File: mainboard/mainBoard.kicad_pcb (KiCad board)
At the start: 4 copper layers, 110 x 75 mm, 85 parts, among them IC1 TCAN3414DR, J1 XT60PW-M, J10 XT30U-M, J11 XT30U-M, J12 Conn_01x03, J13 BM02B-SRSS-TB, J14 BM02B-SRSS-TB, J15 BM02B-SRSS-TB, J16 BM04B-SRSS-TB, J17 BM04B-SRSS-TB, J18 BM04B-SRSS-TB, J19 BM04B-SRSS-TB, J2 XT60PW-M, J20 BM04B-SRSS-TB, J21 B2B-PH_K, J22 Conn_01x02, J23 Conn_02x04_Odd_Even, J24 BM02B-SRSS-TB, J25 BM02B-SRSS-TB, J26 BM02B-SRSS-TB, J3 XT30PW-M, J4 XT30PW-M, J5 Barrel_Jack, J6 XT30U_M, J7 XT30U-M, J8 XT30U-M, J9 XT30U-M, Q1 FQD11P06TM, Q2 FQD11P06TM, U1 TPS565208, U2 TPS565208, U3 TCA9548APWR

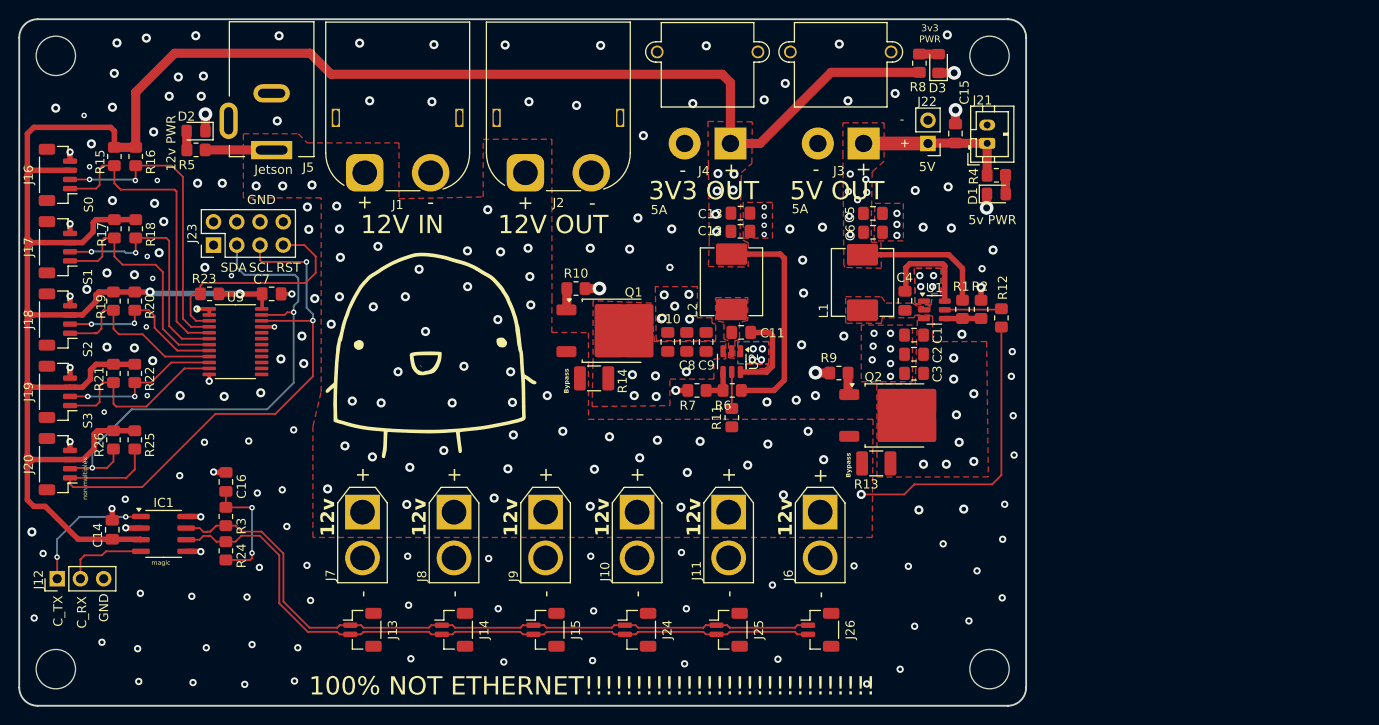
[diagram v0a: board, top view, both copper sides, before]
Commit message: layed out PCB, started routing of mainboard
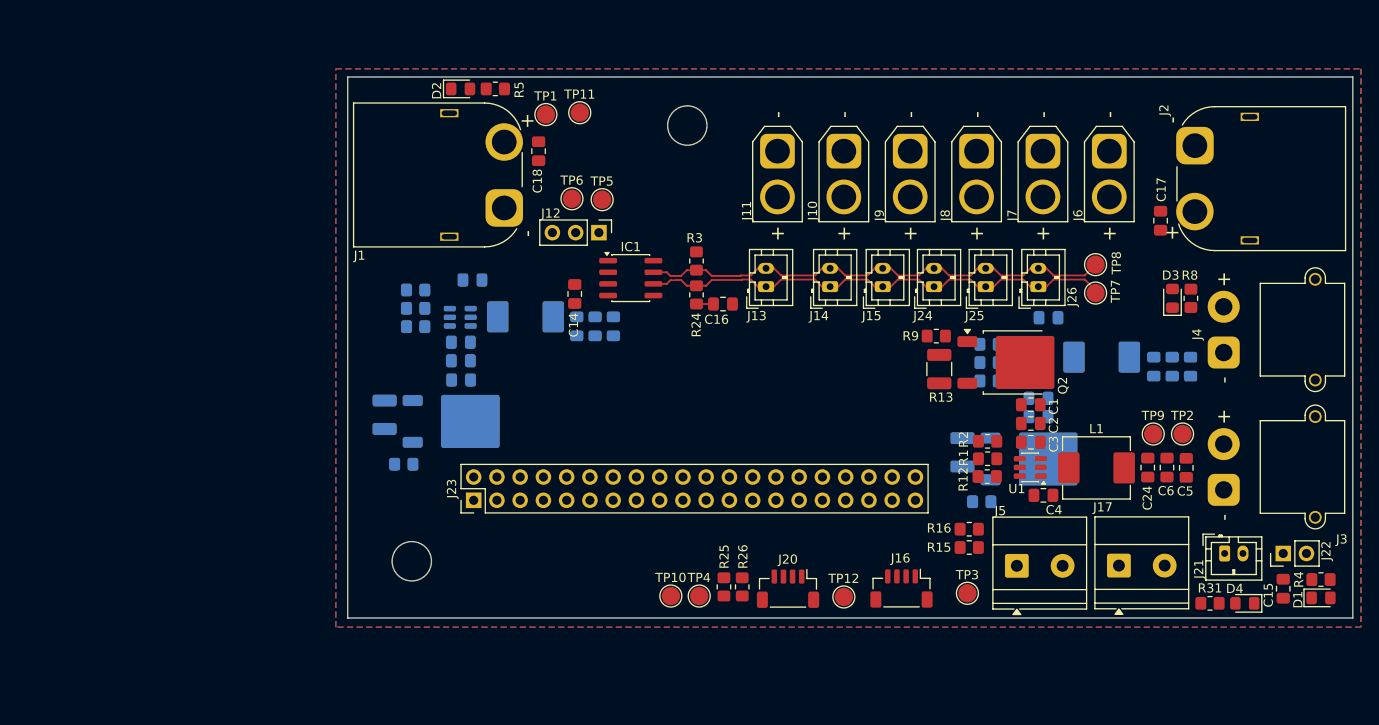
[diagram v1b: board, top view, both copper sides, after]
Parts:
- removed G*** (x2): LOGO, LOGO
- removed H3, H4: M4, MountingHole:MountingHole_4.3mm_M4_DIN965
- removed J18, J19: BM04B-SRSS-TB, Connector_JST:JST_SH_BM04B-SRSS-TB_1x04-1MP_P1.00mm_Vertical
- removed L2: 2.2uH, Inductor_SMD:L_Abracon_ASPI-0630LR
- removed R17, R18, R19, R20, R21, R22: 4.7K, Resistor_SMD:R_0805_2012Metric_Pad1.20x1.40mm_HandSolder
- added C17: 10uF, Capacitor_SMD:C_0805_2012Metric_Pad1.18x1.45mm_HandSolder, F.Cu at (140.2, 41.8)
- added C18: 10uF, Capacitor_SMD:C_0805_2012Metric_Pad1.18x1.45mm_HandSolder, F.Cu at (72.2, 34.2)
- added C19: 10uF, Capacitor_SMD:C_0805_2012Metric_Pad1.18x1.45mm_HandSolder, B.Cu at (63.7, 57.1)
- added C20: 0.1uF, Capacitor_SMD:C_0805_2012Metric_Pad1.18x1.45mm_HandSolder, B.Cu at (63.7, 55.1)
- added C21: 0.1uF, Capacitor_SMD:C_0805_2012Metric_Pad1.18x1.45mm_HandSolder, B.Cu at (65.0, 48.3)
- added C22: 22uF, Capacitor_SMD:C_0805_2012Metric_Pad1.18x1.45mm_HandSolder, B.Cu at (76.4, 53.4)
- added C23: 22uF, Capacitor_SMD:C_0805_2012Metric_Pad1.18x1.45mm_HandSolder, B.Cu at (78.4, 53.4)
- added C24: 22uF, Capacitor_SMD:C_0805_2012Metric_Pad1.18x1.45mm_HandSolder, F.Cu at (138.8, 68.8)
- added C25: 22uF, Capacitor_SMD:C_0805_2012Metric_Pad1.18x1.45mm_HandSolder, B.Cu at (80.4, 53.4)
- added C26: 22uF, Capacitor_SMD:C_0805_2012Metric_Pad1.18x1.45mm_HandSolder, B.Cu at (143.5, 57.8)
- added D4: LED, Diode_SMD:D_0805_2012Metric_Pad1.15x1.40mm_HandSolder, F.Cu at (149.4, 83.6)
- added L3: 2.2uH, Inductor_SMD:L_Abracon_ASPI-0630LR, B.Cu at (133.7, 56.7)
- added L5: 3.3uH, Inductor_SMD:L_Abracon_ASPI-0630LR, B.Cu at (70.8, 52.3)
- added Q3: FQD11P06TM, Package_TO_SOT_SMD:TO-252-2, B.Cu at (63.5, 63.7)
- added R27: 100, Resistor_SMD:R_0805_2012Metric_Pad1.20x1.40mm_HandSolder, B.Cu at (57.5, 68.4)
- added R28: 10K, Resistor_SMD:R_0805_2012Metric_Pad1.20x1.40mm_HandSolder, B.Cu at (58.8, 49.4)
- added R29: 10K, Resistor_SMD:R_0805_2012Metric_Pad1.20x1.40mm_HandSolder, B.Cu at (58.8, 53.4)
- added R30: 87370, Resistor_SMD:R_0805_2012Metric_Pad1.20x1.40mm_HandSolder, B.Cu at (58.8, 51.4)
- added R31: 1K, Resistor_SMD:R_0805_2012Metric_Pad1.20x1.40mm_HandSolder, F.Cu at (145.6, 83.6)
- added TP1: TestPoint_Probe, TestPoint:TestPoint_Pad_D2.0mm, F.Cu at (73.0, 30.2)
- added TP10: TestPoint_Probe, TestPoint:TestPoint_Pad_D2.0mm, F.Cu at (86.7, 82.8)
- added TP11: TestPoint_Probe, TestPoint:TestPoint_Pad_D2.0mm, F.Cu at (76.7, 30.0)
- added TP12: TestPoint_Probe, TestPoint:TestPoint_Pad_D2.0mm, F.Cu at (105.6, 82.9)
- added TP2: TestPoint_Probe, TestPoint:TestPoint_Pad_D2.0mm, F.Cu at (142.6, 65.1)
- added TP3: TestPoint_Probe, TestPoint:TestPoint_Pad_D2.0mm, F.Cu at (119.1, 82.5)
- added TP4: TestPoint_Probe, TestPoint:TestPoint_Pad_D2.0mm, F.Cu at (89.8, 82.8)
- added TP5: TestPoint_Probe, TestPoint:TestPoint_Pad_D2.0mm, F.Cu at (79.2, 39.5)
- added TP6: TestPoint_Probe, TestPoint:TestPoint_Pad_D2.0mm, F.Cu at (75.9, 39.4)
- added TP7: TestPoint_Probe, TestPoint:TestPoint_Pad_D2.0mm, F.Cu at (133.1, 49.7)
- added TP8: TestPoint_Probe, TestPoint:TestPoint_Pad_D2.0mm, F.Cu at (133.1, 46.6)
- added TP9: TestPoint_Probe, TestPoint:TestPoint_Pad_D2.0mm, F.Cu at (139.4, 65.1)
- C10, C11, C12, C13, C8, C9, Q1, R10, R11, R14, R6, R7, U2: moved to B.Cu
- C7: value 0.1uF -> 10uF; moved to B.Cu
- J12: value Conn_01x03 -> CAN Connector
- J13, J14, J15, J24, J25, J26: value BM02B-SRSS-TB -> B2B-PH-K; footprint Connector_JST:JST_SH_BM02B-SRSS-TB_1x02-1MP_P1.00mm_Vertical -> Connector_JST:JST_PH_B2B-PH-K_1x02_P2.00mm_Vertical
- J17: value BM04B-SRSS-TB -> 2 pin screw; footprint Connector_JST:JST_SH_BM04B-SRSS-TB_1x04-1MP_P1.00mm_Vertical -> TerminalBlock_Phoenix:TerminalBlock_Phoenix_MKDS-1,5-2_1x02_P5.00mm_Horizontal
- J23: value Conn_02x04_Odd_Even -> Jertson Header; footprint Connector_PinHeader_2.54mm:PinHeader_2x04_P2.54mm_Vertical -> Connector_PinHeader_2.54mm:PinHeader_2x20_P2.54mm_Vertical
- J5: value Barrel_Jack -> 2 pin screw; footprint Connector_BarrelJack:BarrelJack_Kycon_KLDX-0202-xC_Horizontal -> TerminalBlock_Phoenix:TerminalBlock_Phoenix_MKDS-1,5-2_1x02_P5.00mm_Horizontal
- R23: value 10K -> 0; footprint Resistor_SMD:R_0805_2012Metric_Pad1.20x1.40mm_HandSolder -> Resistor_SMD:R_1210_3225Metric_Pad1.30x2.65mm_HandSolder; moved to B.Cu
- R4: value 150 -> 500
- R8: value 68 -> 300
- U3: value TCA9548APWR -> TPS565208; footprint Package_SO:TSSOP-24_4.4x7.8mm_P0.65mm -> Package_TO_SOT_SMD:SOT-23-6; moved to B.Cu
- moved J17 121.0 mm to (135.6, 79.5), turned to 0 degrees
- moved R15 102.7 mm to (119.3, 77.5), turned to 180 degrees
- moved J16 102.6 mm to (111.9, 82.0), turned to 180 degrees
- moved R16 99.8 mm to (119.3, 75.5), turned to 180 degrees
- moved J5 93.2 mm to (124.5, 79.5), turned to 0 degrees
- moved J7 84.1 mm to (127.3, 34.2)
- moved J20 80.9 mm to (99.5, 82.0), turned to 180 degrees
- moved J2 73.2 mm to (143.9, 33.6), turned to -90 degrees
- moved R26 70.5 mm to (94.5, 81.8), turned to 90 degrees
- moved J12 70.2 mm to (78.8, 43.1), turned to -90 degrees
- moved J8 69.4 mm to (120.1, 34.2)
- moved H1 67.5 mm to (58.4, 79.0)
- moved R25 66.3 mm to (92.5, 81.8), turned to 90 degrees
- moved C15 61.3 mm to (153.6, 82.0), turned to 90 degrees
- moved J22 59.3 mm to (153.6, 78.2), turned to 90 degrees
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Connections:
- C7 pad 1: +3V3 -> Net-(Q3-S)
- J1 pad 1: +12V -> GND
- J1 pad 2: GND -> +12V
- J10 pad 1: +12V -> GND
- J10 pad 2: GND -> +12V
- J11 pad 1: +12V -> GND
- J11 pad 2: GND -> +12V
- J13 pad 1: CANP -> CANN
- J13 pad 2: CANN -> CANP
- J14 pad 1: CANP -> CANN
- J14 pad 2: CANN -> CANP
- J15 pad 1: CANP -> CANN
- J15 pad 2: CANN -> CANP
- J16 pad 1: SCLS0 -> SCL0
- J16 pad 2: SDAS0 -> SDA0
- J17 pad 1: SCLS1 -> 7.4V
- J17 pad 2: SDAS1 -> GND
- J2 pad 1: +12V -> GND
- J2 pad 2: GND -> +12V
- J23 pad 7: GPIO_GCLK -> unconnected-(J23-Pin_7-Pad7)
- J24 pad 1: CANP -> CANN
- J24 pad 2: CANN -> CANP
- J25 pad 1: CANP -> CANN
- J25 pad 2: CANN -> CANP
- J26 pad 1: CANP -> CANN
- J26 pad 2: CANN -> CANP
- J3 pad 1: +5V -> GND
- J3 pad 2: GND -> +5V
- J4 pad 1: +3V3 -> GND
- J4 pad 2: GND -> +3V3
- J5 pad 1: +12V -> 7.4V
- J6 pad 1: +12V -> GND
- J6 pad 2: GND -> +12V
- J7 pad 1: +12V -> GND
- J7 pad 2: GND -> +12V
- J8 pad 1: +12V -> GND
- J8 pad 2: GND -> +12V
- J9 pad 1: +12V -> GND
- J9 pad 2: GND -> +12V
- R15 pad 2: SCLS0 -> SCL0
- R16 pad 2: SDAS0 -> SDA0
- R23 pad 1: +3V3 -> Net-(Q3-S)
- R23 pad 2: GPIO_GCLK -> +12V
- U3 pad 2: GND -> Net-(U3-SW)
- U3 pad 3: GPIO_GCLK -> Net-(Q3-S)
- U3 pad 4: SDAS0 -> Net-(U3-VFB)
- U3 pad 5: SCLS0 -> Net-(U3-EN)
- U3 pad 6: SDAS1 -> Net-(U3-VBST)
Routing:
- net +3V3: track 281.5 -> 0.00 mm, vias 8 -> 0
- net SCL1: track 67.3 -> 0.00 mm, vias 2 -> 0
- net SDA1: track 58.4 -> 0.00 mm, vias 2 -> 0
- net +12V: track 39.6 -> 0.00 mm, vias 55 -> 0
- net SCLS0: track 34.3 -> 0.00 mm
- net SDAS0: track 33.2 -> 0.00 mm, vias 2 -> 0
- net +5V: track 31.9 -> 0.00 mm, vias 7 -> 0
- net GND: track 30.5 -> 0.00 mm, vias 189 -> 0
- net SCLS1: track 26.9 -> 0.00 mm
- net SDAS1: track 26.9 -> 0.00 mm, vias 2 -> 0
- net GPIO_GCLK: track 25.5 -> 0.00 mm
- net CANP: track 77.3 -> 53.4 mm
- net CANN: track 77.3 -> 53.7 mm
- net SCLS3: track 21.5 -> 0.00 mm
- net SCLS2: track 20.6 -> 0.00 mm
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- removed copper zone on F.Cu, net +12V
- removed copper zone on F.Cu, net +3V3
- removed copper zone on F.Cu, net +5V
- removed copper zone on F.Cu, net Net-(Q1-S)
- removed copper zone on F.Cu, net Net-(Q2-S)
- removed copper zone on F.Cu, net Net-(U1-SW)
- removed copper zone on F.Cu, net Net-(U2-SW)
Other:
- board size 110 x 75 mm -> 109.8 x 59.1 mm
- board text removed: "+"
- board text removed: "-"
- board text removed: "100% NOT ETHERNET!!!!!!!!!!!!!!!!!!!!!!!!!!!!!"
- board text removed: "12V IN"
- board text removed: "12V OUT"
- board text removed: "12v"
- board text removed: "12v PWR"
- board text removed: "3V3 OUT"
- board text removed: "3v3 PWR"
- board text removed: "5A"
- board text removed: "5V"
- board text removed: "5V OUT"
- board text removed: "5v PWR"
- board text removed: "Bypass"
- board text removed: "C_RX"
- board text removed: "C_TX"
- board text removed: "GND"
- board text removed: "JC (yetanotheryay)"
- board text removed: "Jetson"
- board text removed: "Main Board"
- board text removed: "RST"
- board text removed: "S0"
- board text removed: "S1"
- board text removed: "S2"
- board text removed: "S3"
- board text removed: "SCL"
- board text removed: "SDA"
- board text removed: "SP (BigPierogi)"
- board text removed: "V2"
- board text removed: "magic"
- board text removed: "non multiplex"

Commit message: finished work on mainboard
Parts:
- added G***: LOGO, LOGO, F.Cu at (93.5, 62.5)
- added G***: LOGO, LOGO, B.Cu at (64.3, 56.1)
- C19, C20, C21, C22, C23, C25, C7, L5, Q3, R23, R27, R28, R29, R30, U3: moved to F.Cu
- moved R27 22.3 mm to (58.8, 46.1)
- moved C21 17.1 mm to (66.3, 65.3)
- moved R28 15.8 mm to (60.1, 65.1)
- moved Q3 13.0 mm to (64.9, 50.8)
- moved R30 11.8 mm to (60.1, 63.1)
- moved R23 11.6 mm to (56.7, 51.5), turned to -90 degrees
- moved L5 9.99 mm to (72.1, 62.2)
- moved U3 9.89 mm to (65.0, 62.2)
- moved C22 7.94 mm to (77.7, 61.2), turned to 90 degrees
- moved C23 7.94 mm to (79.7, 61.2), turned to 90 degrees
- moved C25 7.94 mm to (81.7, 61.2), turned to 90 degrees
- moved R29 7.86 mm to (60.1, 61.1)
- moved J23 4.76 mm to (60.4, 72.2)
- moved C20 4.56 mm to (65.1, 59.4)
- moved C7 4.12 mm to (65.1, 55.3)
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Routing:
- net +3V3: track 0.00 -> 216.4 mm, vias 0 -> 7
- net 7.4V: track 0.00 -> 132.5 mm, vias 0 -> 2
- net +5V: track 0.00 -> 64.0 mm, vias 0 -> 1
- net SDA0: track 0.00 -> 52.2 mm, vias 0 -> 1
- net +12V: track 0.00 -> 48.7 mm, vias 0 -> 34
- net SCL1: track 0.00 -> 48.6 mm, vias 0 -> 2
- net SDA1: track 0.00 -> 48.5 mm
- net SCL0: track 0.00 -> 44.2 mm, vias 0 -> 2
- net C_RX: track 0.00 -> 16.0 mm
- net GND: track 0.00 -> 11.0 mm, vias 0 -> 121
- net Net-(C16-Pad1): track 1.86 -> 12.4 mm, vias 0 -> 2
- net C_TX: track 0.00 -> 7.23 mm
- net Net-(U2-VFB): track 0.00 -> 5.14 mm
- net Net-(U3-EN): track 0.00 -> 5.09 mm
- net Net-(U3-VFB): track 0.00 -> 4.76 mm
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- added copper zone on B.Cu, net +12V
- added copper zone on F.Cu, net +12V
- added copper zone on B.Cu, net +3V3
- added copper zone on F.Cu, net +3V3
- added copper zone on B.Cu, net +5V
- added copper zone on F.Cu, net +5V
- added copper zone on B.Cu, net Net-(Q1-S)
- added copper zone on F.Cu, net Net-(Q2-S)
- added copper zone on F.Cu, net Net-(Q3-S)
- added copper zone on F.Cu, net Net-(U1-SW)
- added copper zone on B.Cu, net Net-(U2-SW)
- added copper zone on F.Cu, net Net-(U3-SW)
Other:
- board text added: "Created by: Sylvester Pudelko (BigPierogi)"

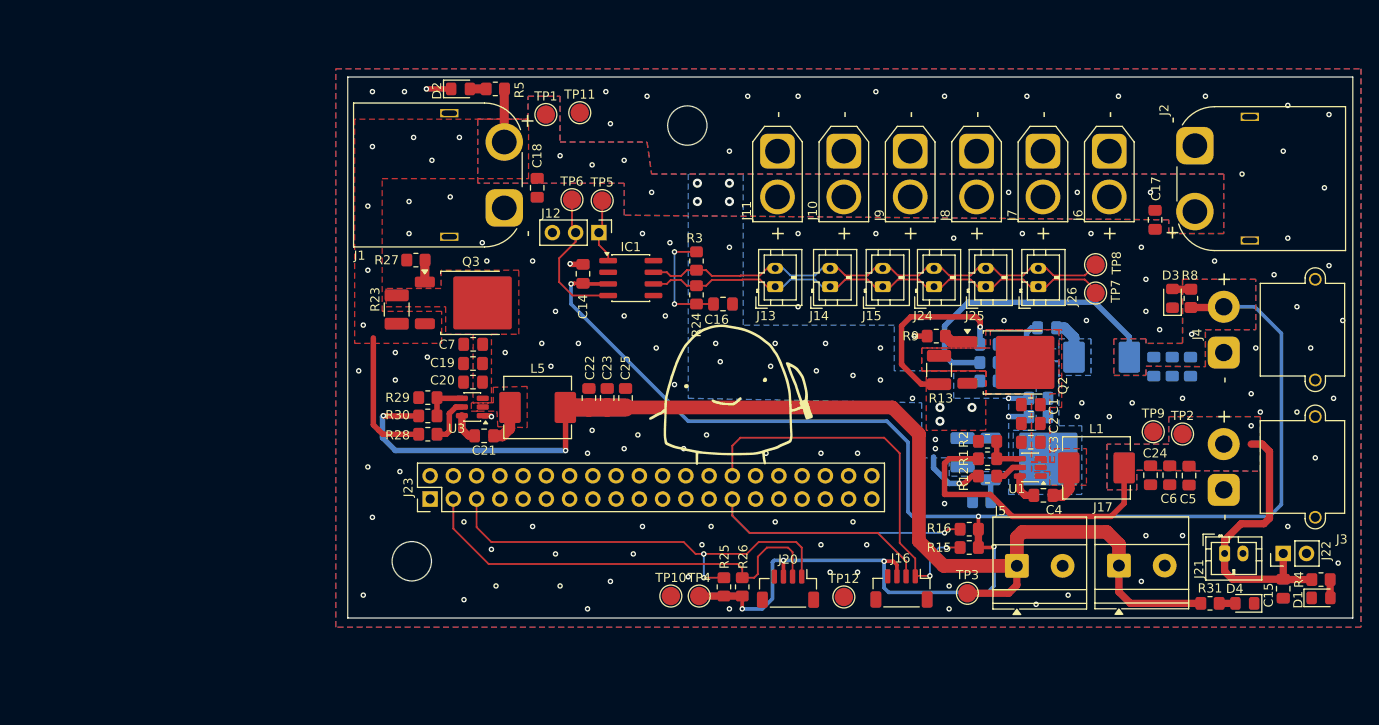
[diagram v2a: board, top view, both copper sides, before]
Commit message: added some capacitors
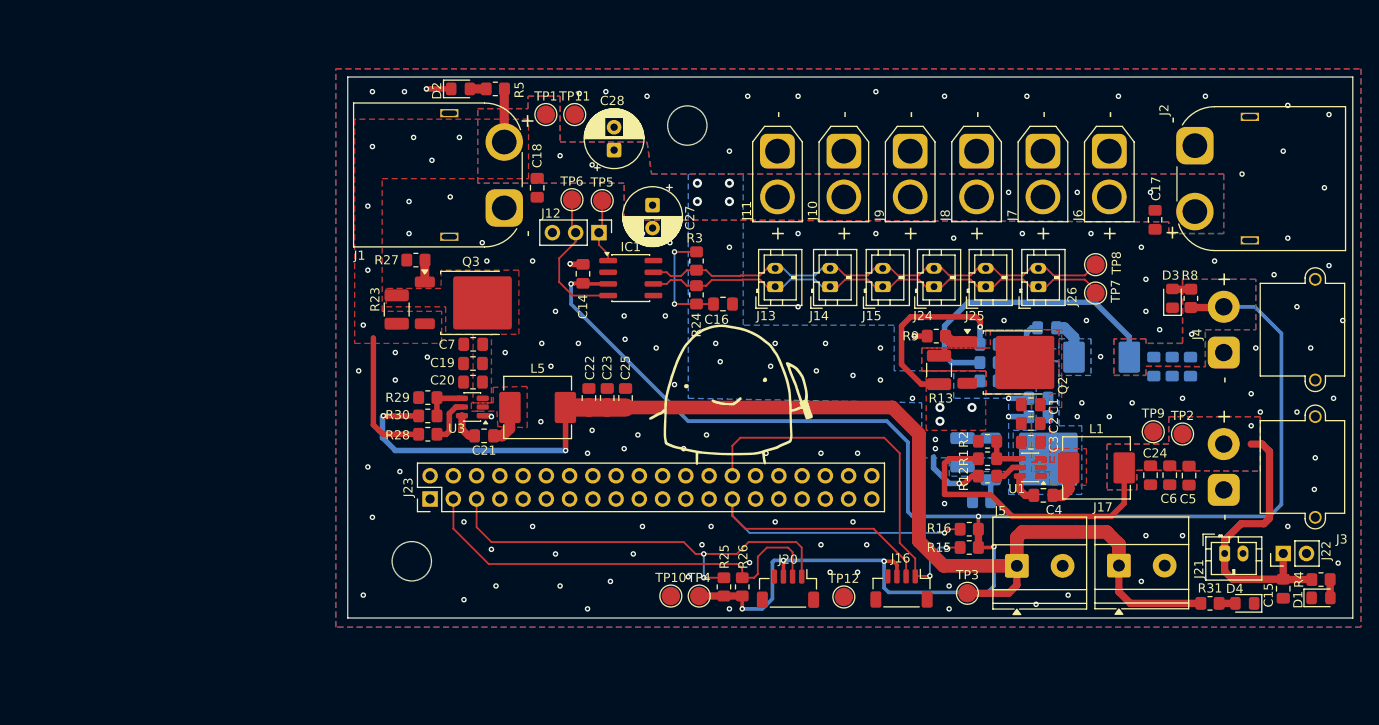
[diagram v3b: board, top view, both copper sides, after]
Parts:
- added C27: 220uF, Capacitor_THT:CP_Radial_D6.3mm_P2.50mm, F.Cu at (84.7, 40.1)
- added C28: 220uF, Capacitor_THT:CP_Radial_D6.3mm_P2.50mm, F.Cu at (80.5, 34.1)
- moved TP11 0.59 mm to (76.2, 30.2)
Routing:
- net GND: vias 121 -> 126
- net +12V: vias 34 -> 32

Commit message: did some updating to mainboard, added a demo board
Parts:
- removed C19, C7: 10uF, Capacitor_SMD:C_0805_2012Metric_Pad1.18x1.45mm_HandSolder
- removed C20, C21: 0.1uF, Capacitor_SMD:C_0805_2012Metric_Pad1.18x1.45mm_HandSolder
- removed C22, C23, C25: 22uF, Capacitor_SMD:C_0805_2012Metric_Pad1.18x1.45mm_HandSolder
- removed D4: LED, Diode_SMD:D_0805_2012Metric_Pad1.15x1.40mm_HandSolder
- removed J17, J5: 2 pin screw, TerminalBlock_Phoenix:TerminalBlock_Phoenix_MKDS-1,5-2_1x02_P5.00mm_Horizontal
- removed L5: 3.3uH, Inductor_SMD:L_Abracon_ASPI-0630LR
- removed Q3: FQD11P06TM, Package_TO_SOT_SMD:TO-252-2
- removed R23: 0, Resistor_SMD:R_1210_3225Metric_Pad1.30x2.65mm_HandSolder
- removed R27: 100, Resistor_SMD:R_0805_2012Metric_Pad1.20x1.40mm_HandSolder
- removed R28, R29: 10K, Resistor_SMD:R_0805_2012Metric_Pad1.20x1.40mm_HandSolder
- removed R30: 87370, Resistor_SMD:R_0805_2012Metric_Pad1.20x1.40mm_HandSolder
- removed R31: 1K, Resistor_SMD:R_0805_2012Metric_Pad1.20x1.40mm_HandSolder
- removed TP3: TestPoint_Probe, TestPoint:TestPoint_Pad_D2.0mm
- removed U3: TPS565208, Package_TO_SOT_SMD:SOT-23-6
- R4, R5: value 500 -> 1k
- R8: value 300 -> 1k
- moved R25 41.9 mm to (134.1, 76.8), turned to -90 degrees
- moved R26 37.9 mm to (132.1, 76.8), turned to -90 degrees
- moved TP4 33.1 mm to (122.9, 82.9)
- moved TP10 32.9 mm to (119.6, 82.8)
- moved J16 29.2 mm to (141.1, 82.0)
- moved J20 29.2 mm to (128.7, 82.0)
- moved TP12 29.2 mm to (134.8, 82.9)
- moved G*** 28.5 mm to (65.4, 57.7)
- moved R15 23.2 mm to (142.3, 74.5), turned to -90 degrees
- moved R16 21.0 mm to (140.3, 74.5), turned to -90 degrees
- moved J23 8.40 mm to (63.5, 80.0)
- moved H1 1.32 mm to (57.1, 78.8)
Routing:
- net 7.4V: track 132.5 -> 0.00 mm, vias 2 -> 0
- net SCL1: track 48.6 -> 82.0 mm, vias 2 -> 1
- net +3V3: track 216.4 -> 249.6 mm, vias 7 -> 3
- net SDA1: track 48.5 -> 74.4 mm, vias 0 -> 1
- net SCL0: track 44.2 -> 64.2 mm, vias 2 -> 1
- net +12V: track 48.7 -> 33.9 mm, vias 32 -> 30
- net Net-(U3-EN): track 5.09 -> 0.00 mm
- net Net-(U3-VFB): track 4.76 -> 0.00 mm
- net Net-(U3-SW): track 4.40 -> 0.00 mm
- net Net-(U3-VBST): track 3.16 -> 0.00 mm
- net Net-(Q3-G): track 2.41 -> 0.00 mm
- net SDA0: track 52.2 -> 54.6 mm
- net Net-(D4-A): track 1.77 -> 0.00 mm
- net GND: track 11.0 -> 9.98 mm, vias 126 -> 146
- removed copper zone on F.Cu, net Net-(Q3-S)
- removed copper zone on F.Cu, net Net-(U3-SW)
